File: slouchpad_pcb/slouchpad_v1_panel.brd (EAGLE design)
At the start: 41 x 69 mm, 14 parts

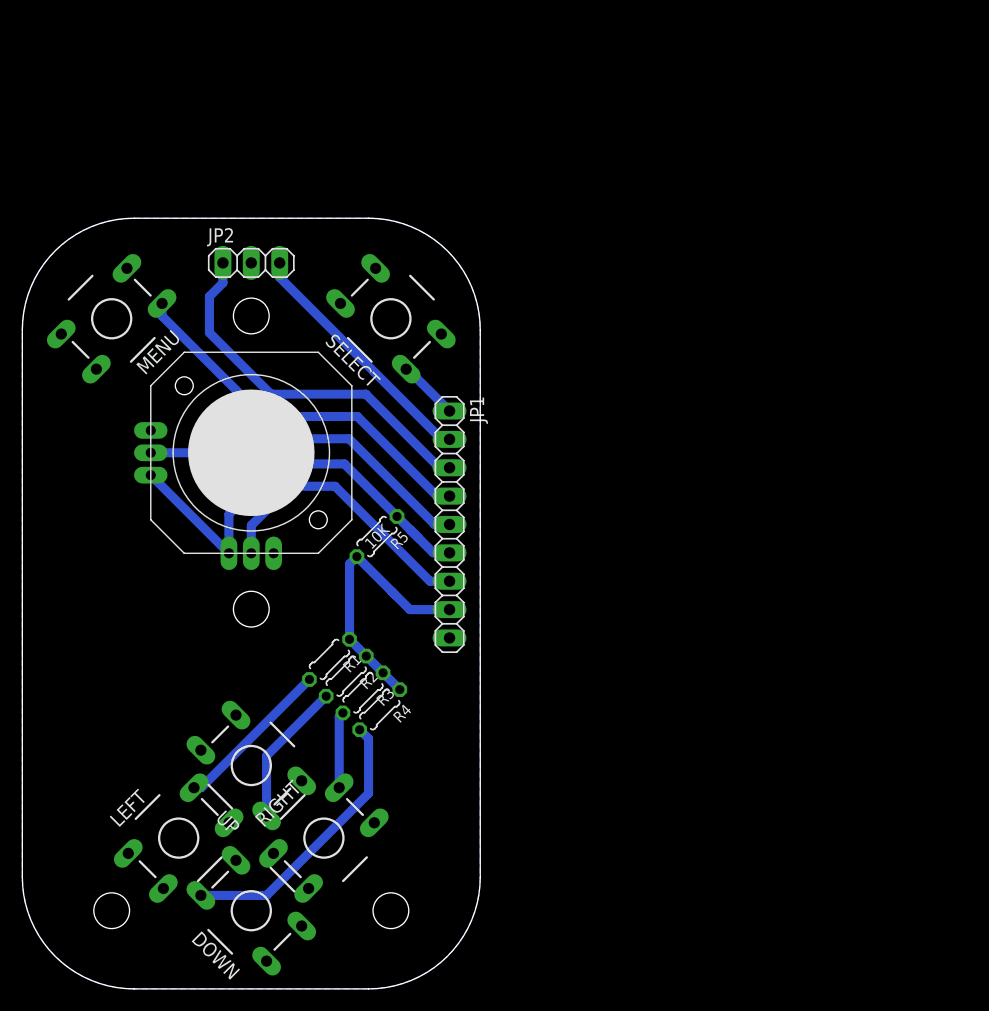
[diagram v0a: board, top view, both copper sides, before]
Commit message: Added dimensions to baord drawings and fixed button 5 position to have correct spacing.
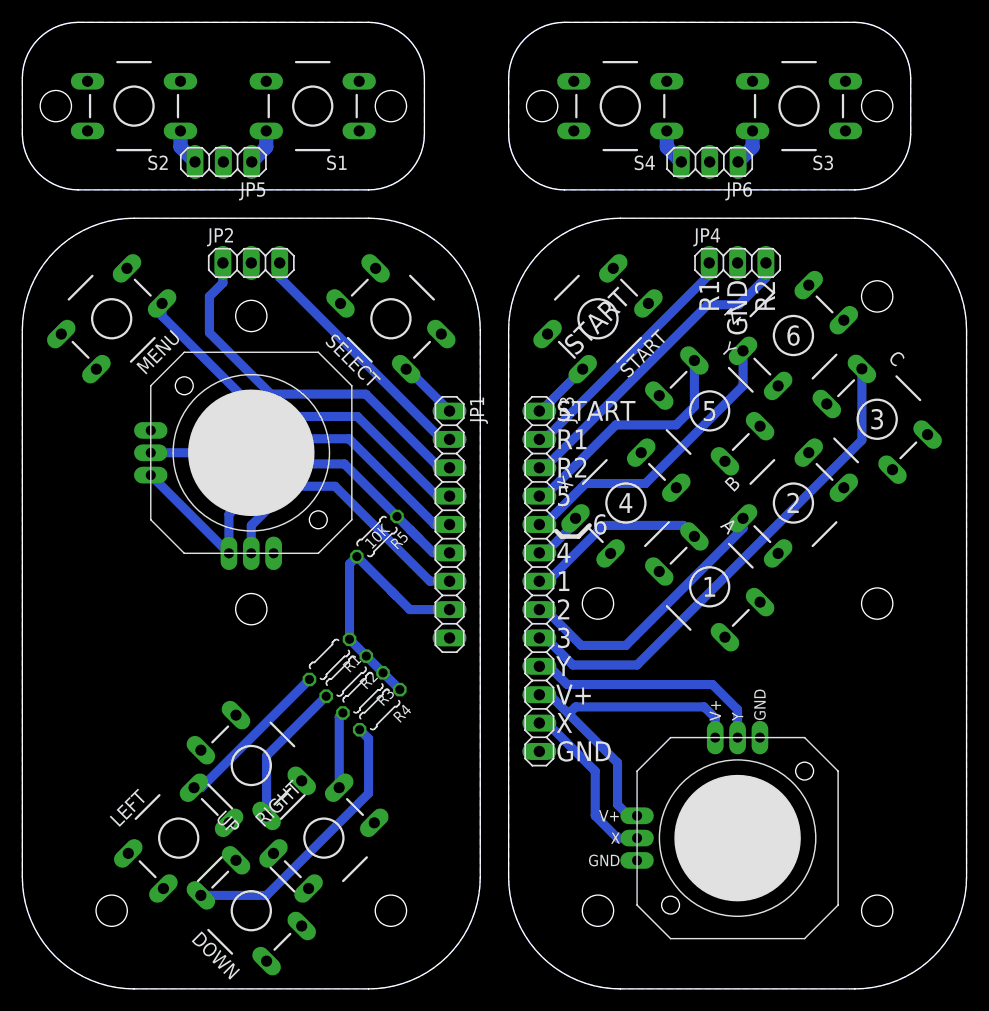
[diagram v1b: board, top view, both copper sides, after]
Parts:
- added A, B, C, S1, S2, S3, S4, START, X, Y, Z: DTS-8, switch-tact:DTS-8
- added JOY2: MICROBUILDER_JOYSTICK_ANALOG_XY, adafruit-minianalogthumb:MICROBUILDER_JOYSTICK_ANALOG_MINITHM
- added JP3: (no value), pinhead:1X13
- added JP4, JP5, JP6: (no value), pinhead:1X03
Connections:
- new net A: A.1, A.2, JP3.7
- new net B: B.1, B.2, JP3.8
- new net C: C.1, C.2, JP3.9
- new net GND1: A.3, A.4, B.3, B.4, C.3, C.4, JOY2.X-, JOY2.Y-, JP3.13, JP4.2, START.3, START.4, X.3, X.4, Y.3, Y.4, Z.3, Z.4
- new net GND2: JP5.2, S1.3, S1.4, S2.3, S2.4
- new net GND3: JP6.2, S3.3, S3.4, S4.3, S4.4
- new net JOYX1: JOY2.X, JP3.12
- new net JOYY1: JOY2.Y, JP3.10
- new net N$7: JP3.2, JP4.1
- new net N$8: JP3.3, JP4.3
- new net S1: JP5.1, S1.1, S1.2
- new net S2: JP5.3, S2.1, S2.2
- new net S3: JP6.1, S3.1, S3.2
- new net S4: JP6.3, S4.1, S4.2
- new net START: JP3.1, START.1, START.2
- new net VCC1: JOY2.X+, JOY2.Y+, JP3.11
- new net X: JP3.6, X.1, X.2
- new net Y: JP3.4, Y.1, Y.2
- new net Z: JP3.5, Z.1, Z.2
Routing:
- net C: track 0.00 -> 44.6 mm
- net VCC1: track 0.00 -> 31.0 mm
- net N$8: track 0.00 -> 28.7 mm
- net Z: track 0.00 -> 26.5 mm
- net B: track 0.00 -> 24.8 mm
- net N$7: track 0.00 -> 22.1 mm
- net JOYY1: track 0.00 -> 21.9 mm
- net Y: track 0.00 -> 21.3 mm
- net A: track 0.00 -> 16.4 mm
- net JOYX1: track 0.00 -> 15.4 mm
- net START: track 0.00 -> 5.43 mm
- net X: track 0.00 -> 4.75 mm
- net S3: track 0.00 -> 3.30 mm
- net S4: track 0.00 -> 3.30 mm
- net S2: track 0.00 -> 3.30 mm
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- added copper zone on layer 16, net GND1
- added copper zone on layer 16, net GND2
- added copper zone on layer 16, net GND3
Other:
- board size 41 x 69 mm -> 84.5 x 86.5 mm
- board text added: "1"
- board text added: "2"
- board text added: "3"
- board text added: "4"
- board text added: "5"
- board text added: "6"
- board text added: "R1"
- board text added: "R2"
- board text added: "START"
